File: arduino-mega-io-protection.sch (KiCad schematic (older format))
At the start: 36 parts, among them J101 CONN_01X02, J102 CONN_01X02, J103 CONN_01X02, J104 CONN_01X02, J105 CONN_01X02, J106 CONN_01X02, J107 CONN_01X02, J108 CONN_01X36, J109 CONN_01X10, J110 CONN_02X18, J111 CONN_01X08, J112 CONN_01X08, J113 CONN_01X08, J114 CONN_01X08, J115 CONN_01X08, J116 CONN_01X02, J117 CONN_01X02, J118 CONN_01X02

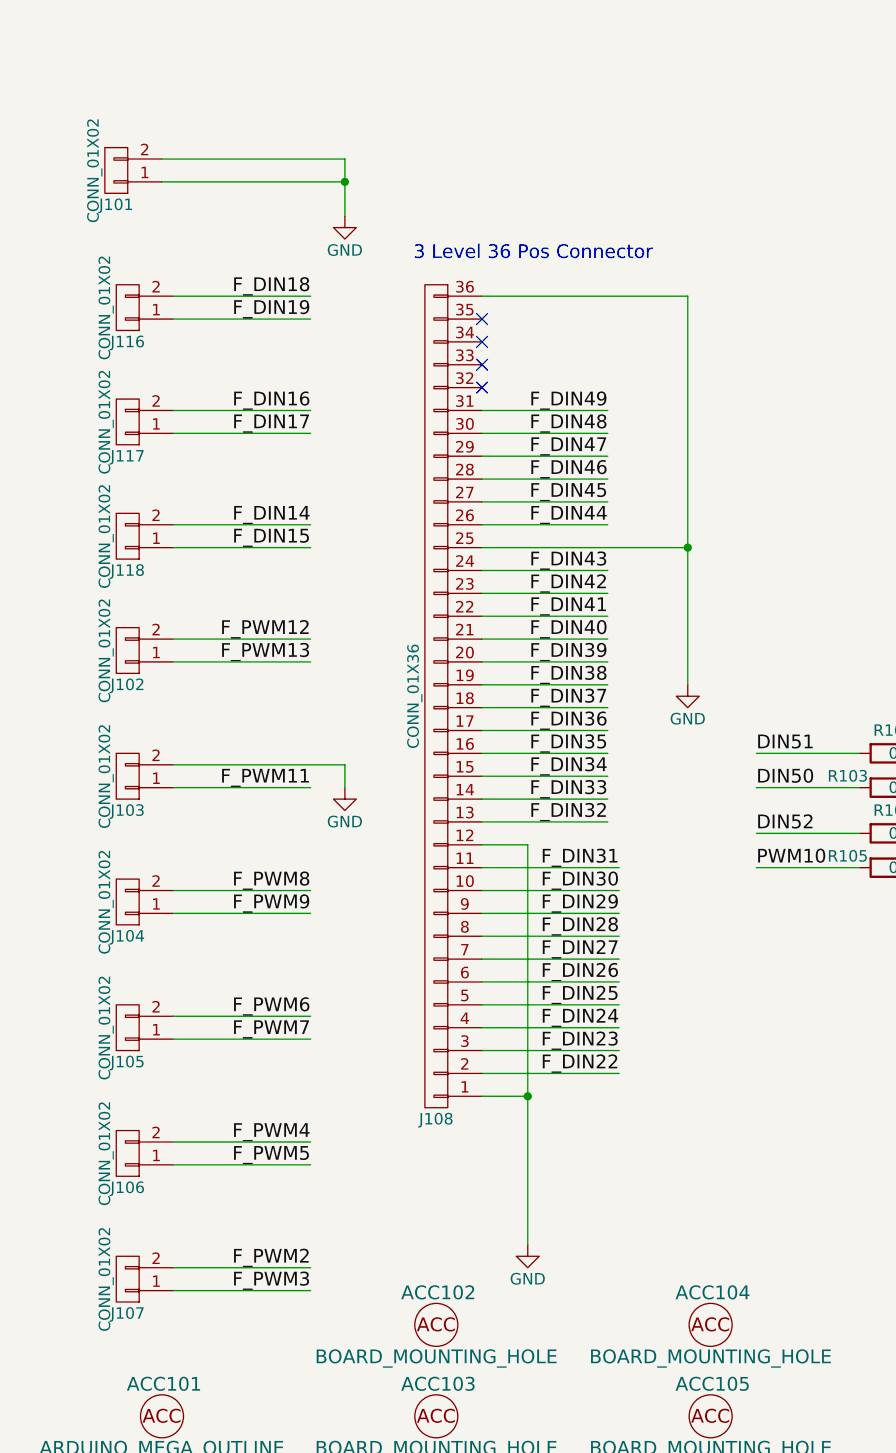
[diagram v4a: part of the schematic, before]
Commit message: adding global hardware library, also fixed some footprint issues and added reverse protection diodes. also cleaned-up design
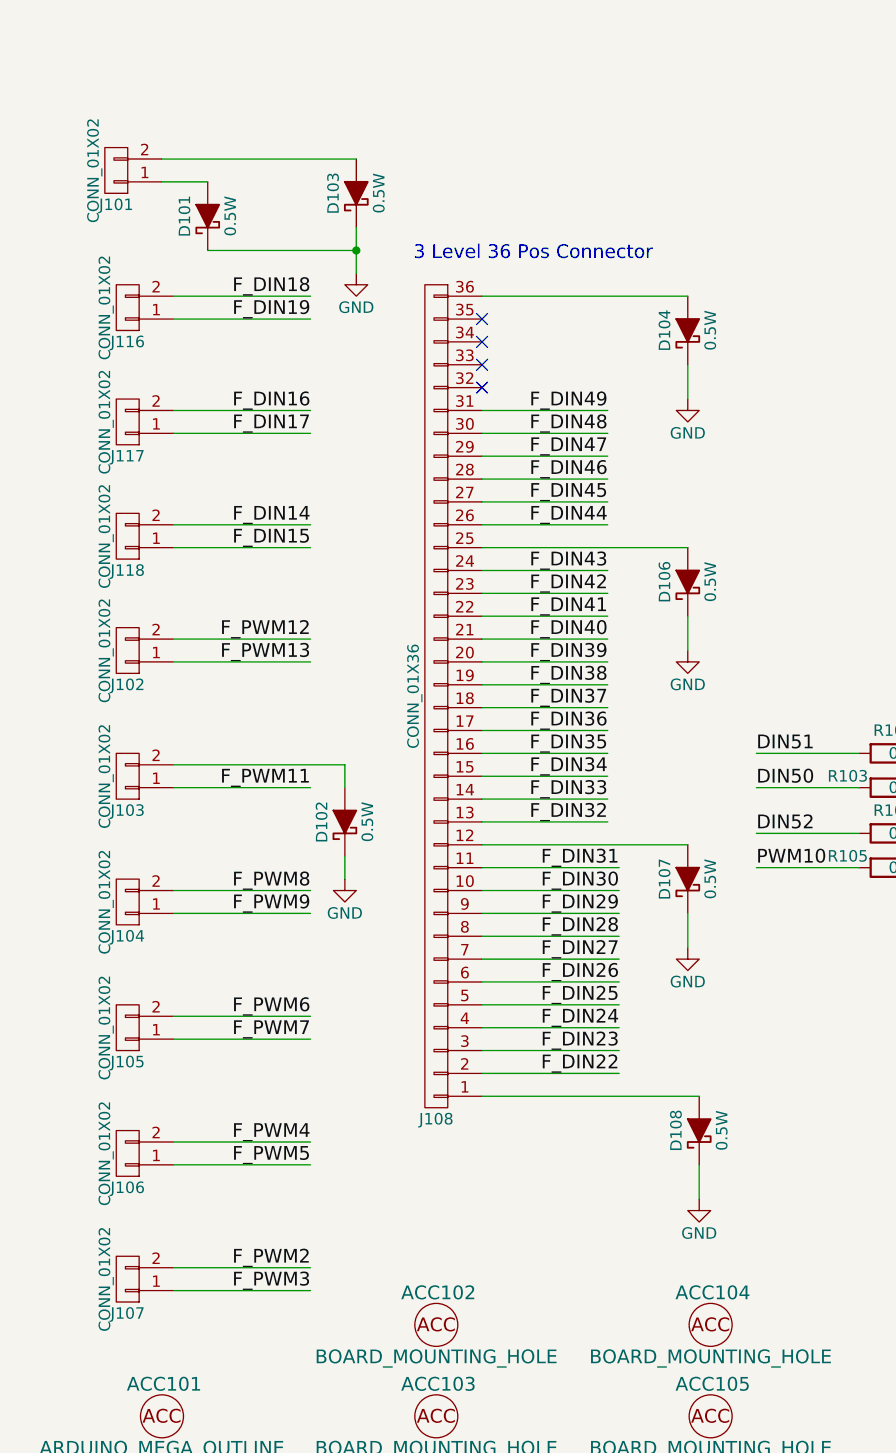
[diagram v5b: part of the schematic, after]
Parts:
- added D101, D102, D103, D104, D106, D107, D108: 0.5W, Diodes_SMD:SOD-123, symbol D_Schottky_ALT
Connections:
- net GND: now also D101.1 (K), D102.1 (K), D103.1 (K), D104.1 (K), D106.1 (K), D107.1 (K), D108.1 (K); no longer J101.1 (P1), J101.2 (P2), J103.2 (P2), J108.1 (P1), J108.12 (P12), J108.25 (P25), J108.36 (P36)
- new net: D108.2 (A), J108.1 (P1)
- new net: D107.2 (A), J108.12 (P12)
- new net: D106.2 (A), J108.25 (P25)
- new net: D104.2 (A), J108.36 (P36)
- new net: D102.2 (A), J103.2 (P2)
- new net: D101.2 (A), J101.1 (P1)
- new net: D103.2 (A), J101.2 (P2)

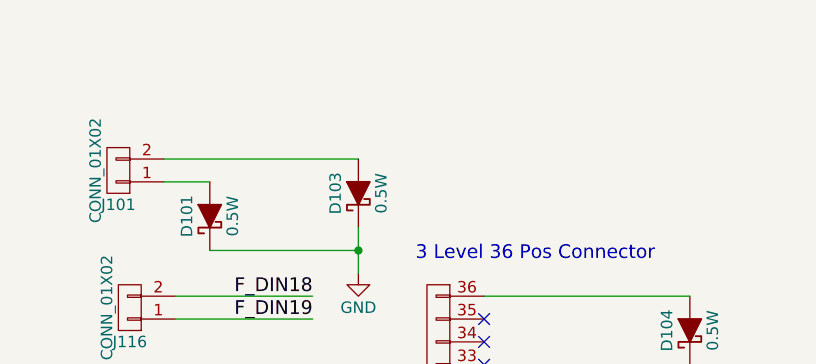
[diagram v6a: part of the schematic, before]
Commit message: fixing some component/BOM part numbers
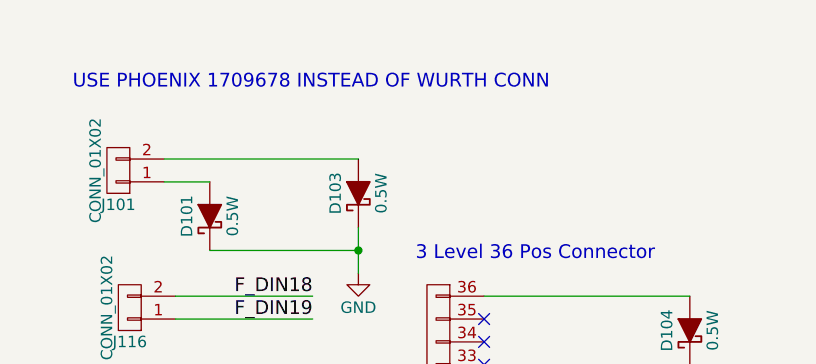
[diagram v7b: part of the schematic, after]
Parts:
- J110: MPN PRPC018DAAN-RC -> X; Populate (none) -> 1
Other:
- note added: "USE PHOENIX 1709678 INSTEAD OF WURTH CONN"
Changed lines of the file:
@@
 F 2 "Pin_Headers:Pin_Header_Straight_2x18_Pitch2.54mm" H 10950 4050 50  0001 C CNN
 F 3 "https://media.digikey.com/PDF/Data%20Sheets/Sullins%20PDFs/xRxCzzzDxxN-RC_11636-B.pdf" H 10950 4050 50  0001 C CNN
-F 4 "PRPC018DAAN-RC" H 10950 5100 60  0001 C CNN "MPN"
-F 5 "Sullins Connector Solutions" H 10950 5100 60  0001 C CNN "MFN"
-F 6 "X" H 10950 5100 60  0001 C CNN "Characteristics"
-F 7 "CONN HEADER .100\" DUAL STR 36POS" H 10950 5100 60  0001 C CNN "Description"
-F 8 "Through Hole" H 10950 5100 60  0001 C CNN "Package ID"
-F 9 "Digikey" H 10950 5100 60  0001 C CNN "Source"
-F 10 "Y" H 10950 5100 60  0001 C CNN "Critical"
-F 11 "X" H 10950 5100 60  0001 C CNN "Notes"
+F 4 "X" H 10950 5100 60  0001 C CNN "Characteristics"
+F 5 "CONN HEADER .100\" DUAL STR 36POS" H 10950 5100 60  0001 C CNN "Description"
+F 6 "Sullins Connector Solutions" H 10950 5100 60  0001 C CNN "MFN"
+F 7 "Through Hole" H 10950 5100 60  0001 C CNN "Package ID"
+F 8 "Digikey" H 10950 5100 60  0001 C CNN "Source"
+F 9 "Y" H 10950 5100 60  0001 C CNN "Critical"
+F 10 "X" H 10950 5100 60  0001 C CNN "Notes"
+F 11 "1" H 10950 5100 60  0001 C CNN "Populate"
+F 12 "X" H 10950 5100 60  0001 C CNN "MPN"
 	1    10950 5100
 	0    1    1    0
@@
 	0    -1   -1   0
 $EndComp
+Text Notes 650  800  0    60   ~ 0
+USE PHOENIX 1709678 INSTEAD OF WURTH CONN
 $EndSCHEMATC

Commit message: updating schematic to look more consistent
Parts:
- removed J101, J102, J103, J104, J105, J106, J107, J116, J117, J118: CONN_01X02, 3ML_Footprint_Library:Wurth_691103010002, symbol CONN_01X02
- added J?: Conn_01x20, symbol Conn_01x20
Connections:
- net F_DIN14: now also J?.7 (Pin_7)
- net F_DIN15: now also J?.8 (Pin_8)
- net F_DIN16: now also J?.5 (Pin_5)
- net F_DIN17: now also J?.6 (Pin_6)
- net F_DIN18: now also J?.3 (Pin_3)
- net F_DIN19: now also J?.4 (Pin_4)
- net F_PWM11: now also J?.12 (Pin_12)
- net F_PWM12: now also J?.9 (Pin_9)
- net F_PWM13: now also J?.10 (Pin_10)
- net F_PWM2: now also J?.19 (Pin_19)
- net F_PWM3: now also J?.20 (Pin_20)
- net F_PWM4: now also J?.17 (Pin_17)
- net F_PWM5: now also J?.18 (Pin_18)
- net F_PWM6: now also J?.15 (Pin_15)
- net F_PWM7: now also J?.16 (Pin_16)
- net F_PWM8: now also J?.13 (Pin_13)
- net F_PWM9: now also J?.14 (Pin_14)
- net GND: now also D101.2 (A), D102.2 (A), D103.2 (A), D104.2 (A), D106.2 (A), D107.2 (A), D108.2 (A); no longer D101.1 (K), D102.1 (K), D103.1 (K), D104.1 (K), D106.1 (K), D107.1 (K), D108.1 (K)
- net at J108.1 (P1): now also D108.1 (K); no longer D108.2 (A)
- net at J108.12 (P12): now also D107.1 (K); no longer D107.2 (A)
- net at J108.25 (P25): now also D106.1 (K); no longer D106.2 (A)
- net at J108.36 (P36): now also D104.1 (K); no longer D104.2 (A)
- new net: D103.1 (K), J?.2 (Pin_2)
- new net: D101.1 (K), J?.1 (Pin_1)
- new net: D102.1 (K), J?.11 (Pin_11)
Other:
- note added: "20 Pos Field Side Connector"
- note added: "Accessories"
- note added: "Arduino Mega 2560 Base Board\nDigital Isolation Only\nArduino snaps into this board\nTOP VIEW\n\n45 Digital Inputs"
- note added: "Field Connections"
- note removed: "Arduino Mega 2560 Base Board\nDigital Isolation Only\nArduino snaps into this board\n\n45 Digital Inputs"
- note removed: "USE PHOENIX 1709678 INSTEAD OF WURTH CONN"
- moved on the sheet: ACC101, ACC102, ACC103, ACC104, ACC105, ACC106, ACC107, ACC108, ACC109, ACC110, ACC111, ACC112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
